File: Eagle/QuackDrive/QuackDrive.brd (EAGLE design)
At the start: 35.9 x 27.9 mm, 102 parts, among them IC1 MCP1703T-3302E/CB, IC10 TB67H450FNG,EL, IC12 TB67H450FNG,EL, IC2 MCP1703T-3302E/CB, IC4 TB67H450FNG,EL, IC6 TB67H450FNG,EL, IC8 TB67H450FNG,EL, Q1 NPN-BJT, Q2 NPN-BJT, U1 MPU-6050-1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

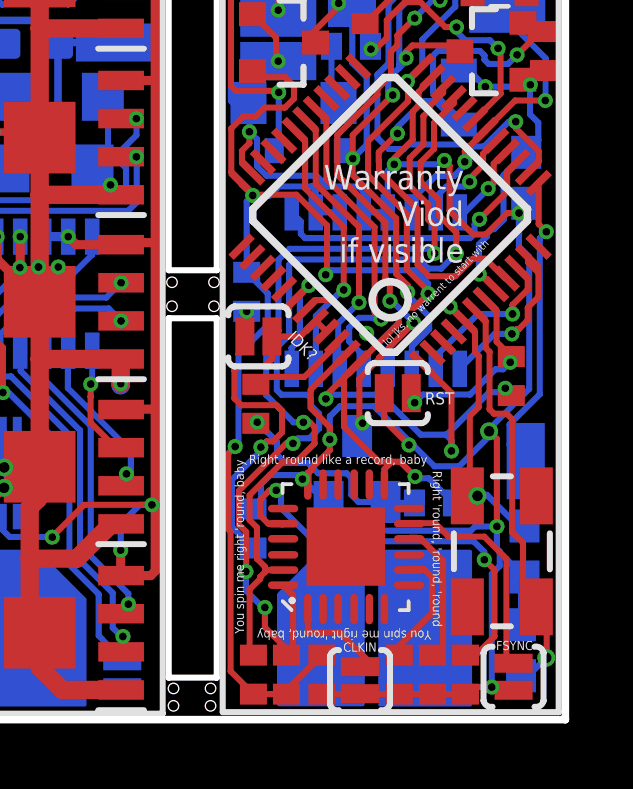
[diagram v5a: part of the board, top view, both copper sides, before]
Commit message: Remove crystal, add Sbus inverter
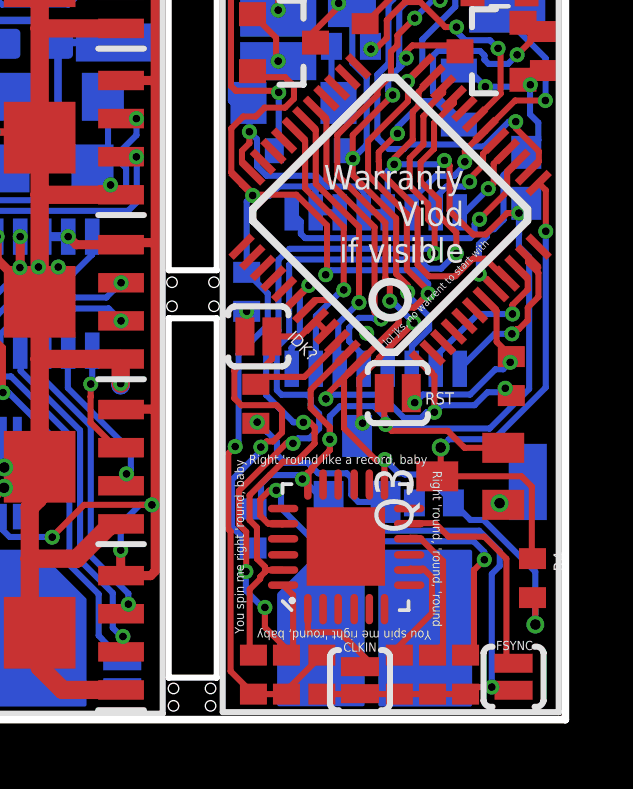
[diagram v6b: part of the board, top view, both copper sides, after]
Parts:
- removed C18, C20: 18pF, SparkFun-Capacitors:0603
- removed OSC: 8MHz, SparkFun2:CRYSTAL-SMD-5X3
- added Q3: (no value), adafruit:SOT23
- added R4: 1k, SparkFun:C0402
- moved PAD23 0.70 mm to (35.6, 9.64)
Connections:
- removed net 8: PAD23.1, UC1.13
- new net N$3: PAD23.1, Q3.1
- new net N$4: Q3.3, R4.1, UC1.13
- net GND: now also Q3.2; no longer C18.1, C20.1
- net OSC_IN: no longer C20.2, OSC.3
- net OSC_OUT: no longer C18.2, OSC.1
- net VCC: now also R4.2
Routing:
- net N$4: track 0.00 -> 18.0 mm, vias 0 -> 2
- net OSC_OUT: track 13.9 -> 0.00 mm, vias 1 -> 0
- net 8: track 10.1 -> 0.00 mm, vias 1 -> 0
- net OSC_IN: track 9.59 -> 0.03 mm, vias 2 -> 0
- net GND: track 104.1 -> 99.6 mm, vias 15 -> 13
- net VCC: track 86.1 -> 89.6 mm, vias 10 -> 11
- net N$3: track 0.00 -> 1.38 mm, vias 0 -> 1

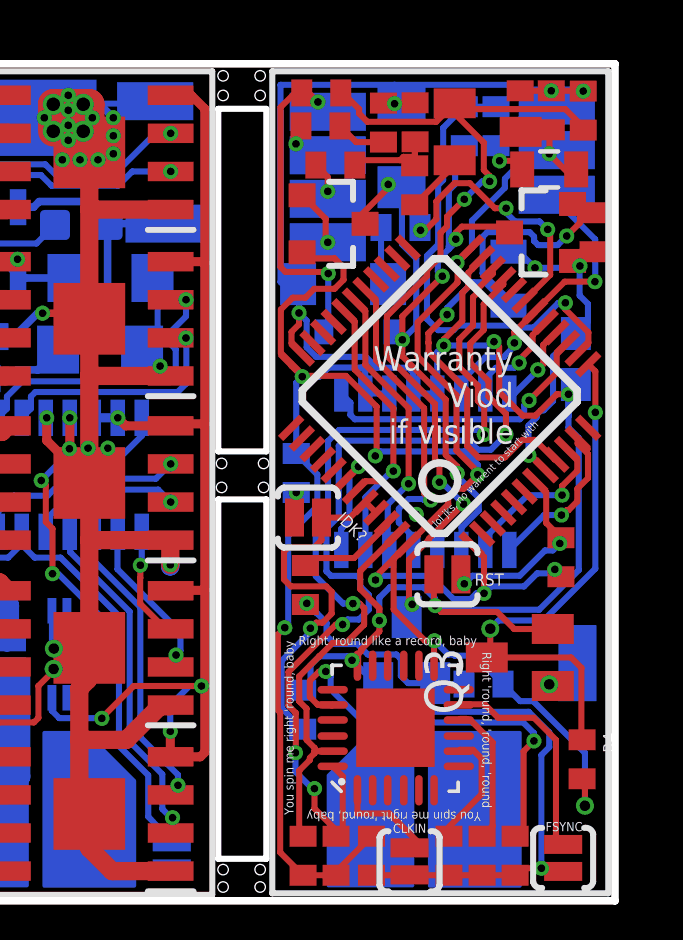
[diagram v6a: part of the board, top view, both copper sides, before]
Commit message: fixed silksceeen
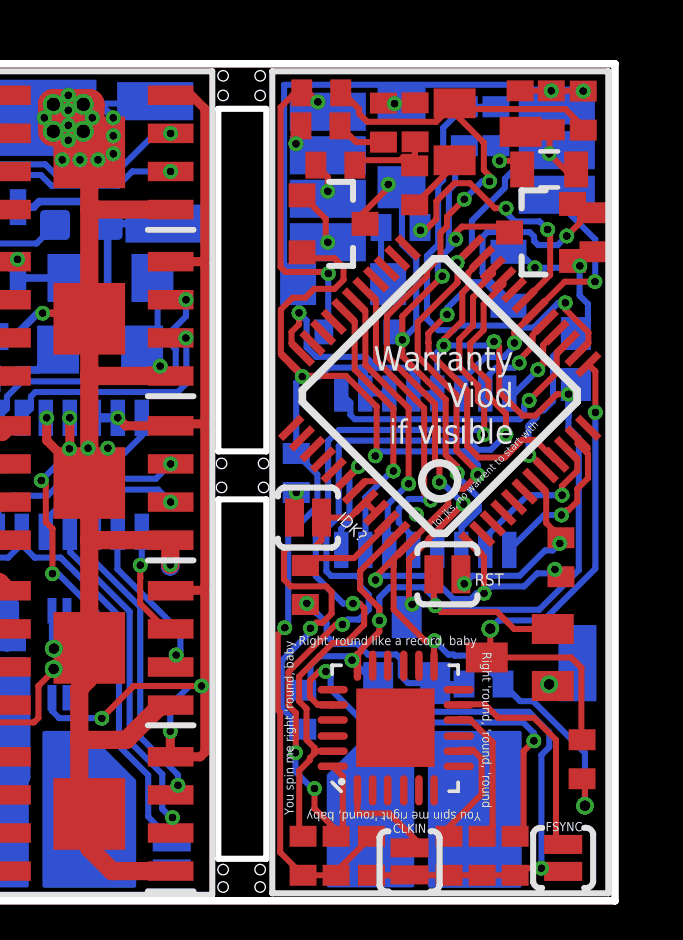
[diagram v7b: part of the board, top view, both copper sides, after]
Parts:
- R4: value 1k -> 4K7
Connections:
- net N$3 renamed SBUSIN
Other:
- board text added: "Never gonna give you up Never gonna let you down Never gonna run around and Never gonna make you cry Never gonna say goodbye Never gonna tell a lie a Never gonna let you Never gonna run ar Never gonna make Never gonna say go Never gonna tell a"
- board text removed: "Never gonna give you up Never gonna let you down Never gonna run around and desert you Never gonna make you cry Never gonna say goodbye Never gonna tell a lie and hurt you Never gonna give you up Never gonna let you down Never gonna run around and desert you Never gonna make you cry Never gonna say goodbye Never gonna tell a lie and hurt you"
- board text removed: "S3G"
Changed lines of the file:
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@@
 <drawing>
 <settings>
-<setting alwaysvectorfont="no"/>
+<setting alwaysvectorfont="yes"/>
 <setting verticaltext="up"/>
 </settings>
@@
 <layer number="15" name="Route15" color="23" fill="1" visible="no" active="no"/>
 <layer number="16" name="Bottom" color="1" fill="1" visible="yes" active="yes"/>
-<layer number="17" name="Pads" color="2" fill="1" visible="yes" active="yes"/>
-<layer number="18" name="Vias" color="2" fill="1" visible="yes" active="yes"/>
-<layer number="19" name="Unrouted" color="6" fill="1" visible="yes" active="yes"/>
-<layer number="20" name="Dimension" color="24" fill="1" visible="yes" active="yes"/>
-<layer number="21" name="tPlace" color="7" fill="1" visible="yes" active="yes"/>
-<layer number="22" name="bPlace" color="7" fill="1" visible="yes" active="yes"/>
-<layer number="23" name="tOrigins" color="15" fill="1" visible="yes" active="yes"/>
-<layer number="24" name="bOrigins" color="15" fill="1" visible="yes" active="yes"/>
+<layer number="17" name="Pads" color="2" fill="1" visible="no" active="yes"/>
+<layer number="18" name="Vias" color="2" fill="1" visible="no" active="yes"/>
+<layer number="19" name="Unrouted" color="6" fill="1" visible="no" active="yes"/>
+<layer number="20" name="Dimension" color="24" fill="1" visible="no" active="yes"/>
+<layer number="21" name="tPlace" color="7" fill="1" visible="no" active="yes"/>
+<layer number="22" name="bPlace" color="7" fill="1" visible="no" active="yes"/>
+<layer number="23" name="tOrigins" color="15" fill="1" visible="no" active="yes"/>
+<layer number="24" name="bOrigins" color="15" fill="1" visible="no" active="yes"/>
 <layer number="25" name="tNames" color="7" fill="1" visible="yes" active="yes"/>
 <layer number="26" name="bNames" color="7" fill="1" visible="yes" active="yes"/>
@@
 <layer number="37" name="tTest" color="7" fill="1" visible="no" active="yes"/>
 <layer number="38" name="bTest" color="7" fill="1" visible="no" active="yes"/>
-<layer number="39" name="tKeepout" color="4" fill="11" visible="yes" active="yes"/>
-<layer number="40" name="bKeepout" color="1" fill="11" visible="yes" active="yes"/>
-<layer number="41" name="tRestrict" color="4" fill="10" visible="yes" active="yes"/>
-<layer number="42" name="bRestrict" color="1" fill="10" visible="yes" active="yes"/>
+<layer number="39" name="tKeepout" color="4" fill="11" visible="no" active="yes"/>
+<layer number="40" name="bKeepout" color="1" fill="11" visible="no" active="yes"/>
+<layer number="41" name="tRestrict" color="4" fill="10" visible="no" active="yes"/>
+<layer number="42" name="bRestrict" color="1" fill="10" visible="no" active="yes"/>
 <layer number="43" name="vRestrict" color="2" fill="10" visible="no" active="yes"/>
 <layer number="44" name="Drills" color="7" fill="1" visible="no" active="yes"/>
@@
 <layer number="49" name="Reference" color="7" fill="1" visible="no" active="yes"/>
 <layer number="50" name="dxf" color="7" fill="1" visible="no" active="no"/>
-<layer number="51" name="tDocu" color="7" fill="1" visible="yes" active="yes"/>
-<layer number="52" name="bDocu" color="7" fill="1" visible="yes" active="yes"/>
+<layer number="51" name="tDocu" color="7" fill="1" visible="no" active="yes"/>
+<layer number="52" name="bDocu" color="7" fill="1" visible="no" active="yes"/>
 <layer number="53" name="tGND_GNDA" color="7" fill="9" visible="no" active="no"/>
 <layer number="54" name="bGND_GNDA" color="1" fill="9" visible="no" active="no"/>
@@
 <hole x="25.1" y="16.3" drill="0.35"/>
 <hole x="25.1" y="15.5" drill="0.35"/>
-<text x="34.85" y="21.74" size="1.016" layer="26" rot="MR90">S3G</text>
 <text x="31.38833125" y="19.842240625" size="1.016" layer="26" rot="MR270" align="bottom-right">G+-5</text>
 <text x="17.922603125" y="25.8454875" size="0.4064" layer="26" rot="MR0">GROUNDDDD</text>
@@
 <text x="3.91773125" y="12.607525" size="0.4064" layer="26" rot="MR45">Never gonna give you up
 Never gonna let you down
-Never gonna run around and desert you
+Never gonna run around and
 Never gonna make you cry
 Never gonna say goodbye
-Never gonna tell a lie and hurt you Never gonna give you up
-Never gonna let you down
-Never gonna run around and desert you
-Never gonna make you cry
-Never gonna say goodbye
-Never gonna tell a lie and hurt you</text>
+Never gonna tell a lie a
+Never gonna let you
+Never gonna run ar
+Never gonna make
+Never gonna say go
+Never gonna tell a</text>
 <rectangle x1="-0.0127" y1="-0.0127" x2="14.3383" y2="0.0127" layer="201"/>
 <rectangle x1="-0.0127" y1="0.0127" x2="14.3383" y2="0.0381" layer="201"/>
@@
 <attribute name="MF" value="Allegro MicroSystems LLC" x="17.794921875" y="9.938446875" size="1.778" layer="28" rot="MR180" display="off"/>
 <attribute name="MP" value="ACS70331EESATR-005B3" x="17.794921875" y="9.938446875" size="1.778" layer="28" rot="MR180" display="off"/>
-<attribute name="NAME" x="15.254921875" y="7.398446875" size="1.27" layer="26" rot="MR180"/>
 <attribute name="PACKAGE" value="WFQFN-12 Allegro MicroSystems LLC" x="17.794921875" y="9.938446875" size="1.778" layer="28" rot="MR180" display="off"/>
 <attribute name="VALUE" x="15.254921875" y="13.748446875" size="1.27" layer="28" rot="MR180"/>
 </element>
-<element name="R4" library="SparkFun" package="C0402" value="1k" x="35.71654375" y="6.437225" smashed="yes" rot="R270">
-<attribute name="NAME" x="36.41504375" y="7.326225" size="0.4064" layer="25" rot="R270"/>
+<element name="R4" library="SparkFun" package="C0402" value="4K7" x="35.71654375" y="6.437225" smashed="yes" rot="R270">
 <attribute name="VALUE" x="34.57354375" y="7.516725" size="0.4064" layer="27" rot="R270"/>
 </element>
 <element name="Q3" library="adafruit" package="SOT23" value="" x="33.6400875" y="9.831" smashed="yes" rot="R90">
-<attribute name="NAME" x="31.7350875" y="7.926" size="1.27" layer="25" rot="R90"/>
 <attribute name="VALUE" x="36.8150875" y="7.926" size="1.27" layer="27" rot="R90"/>
 </element>
@@
 <via x="34.359928125" y="2.805725" extent="1-16" drill="0.254"/>
 <wire x1="33.718971875" y1="2.805725" x2="33.485" y2="2.571753125" width="0.2032" layer="1"/>
-<wire x1="25.66235" y1="22.34765" x2="25.66235" y2="28.92" width="0.2032" layer="16"/>
+<wire x1="25.784815625" y1="22.277584375" x2="25.784815625" y2="28.92" width="0.2032" layer="16"/>
 <contactref element="U$3" pad="13"/>
 <contactref element="U$3" pad="12"/>
-<wire x1="25.66235" y1="28.92" x2="29.459659375" y2="28.92" width="0.2032" layer="16"/>
+<wire x1="25.784815625" y1="28.92" x2="29.459659375" y2="28.92" width="0.2032" layer="16"/>
 <wire x1="29.459659375" y1="28.92" x2="33.49" y2="28.92" width="0.2032" layer="16"/>
 <wire x1="30.89" y1="18.63" x2="30.09" y2="18.63" width="0.2032" layer="16"/>
@@
 <contactref element="PAD17" pad="1"/>
 <wire x1="27.160046875" y1="23.749953125" x2="27.24" y2="23.67" width="0.2032" layer="16"/>
-<wire x1="26.25" y1="22.277584375" x2="25.732415625" y2="22.277584375" width="0.2032" layer="16"/>
-<wire x1="25.732415625" y1="22.277584375" x2="25.66235" y2="22.34765" width="0.2032" layer="16"/>
+<wire x1="26.25" y1="22.277584375" x2="25.784815625" y2="22.277584375" width="0.2032" layer="16"/>
 <wire x1="28.876290625" y1="9.02" x2="28.92" y2="8.976290625" width="0.2032" layer="16"/>
 <wire x1="28.92" y1="8.976290625" x2="29.876290625" y2="8.02" width="0.2032" layer="16"/>
@@
 <wire x1="3.64" y1="6.75" x2="3.64" y2="7.015" width="0.2032" layer="16"/>
 </signal>
-<signal name="N$3">
+<signal name="SBUSIN">
 <contactref element="PAD23" pad="1"/>
 <contactref element="Q3" pad="1"/>

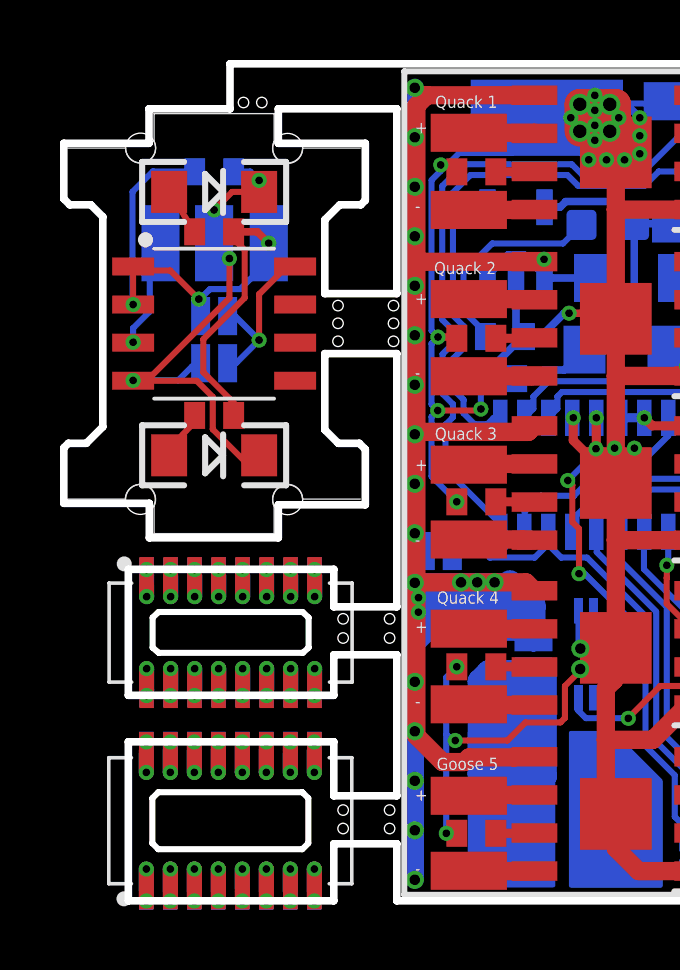
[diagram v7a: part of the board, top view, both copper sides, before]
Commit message: Removed castleation on raiser boards
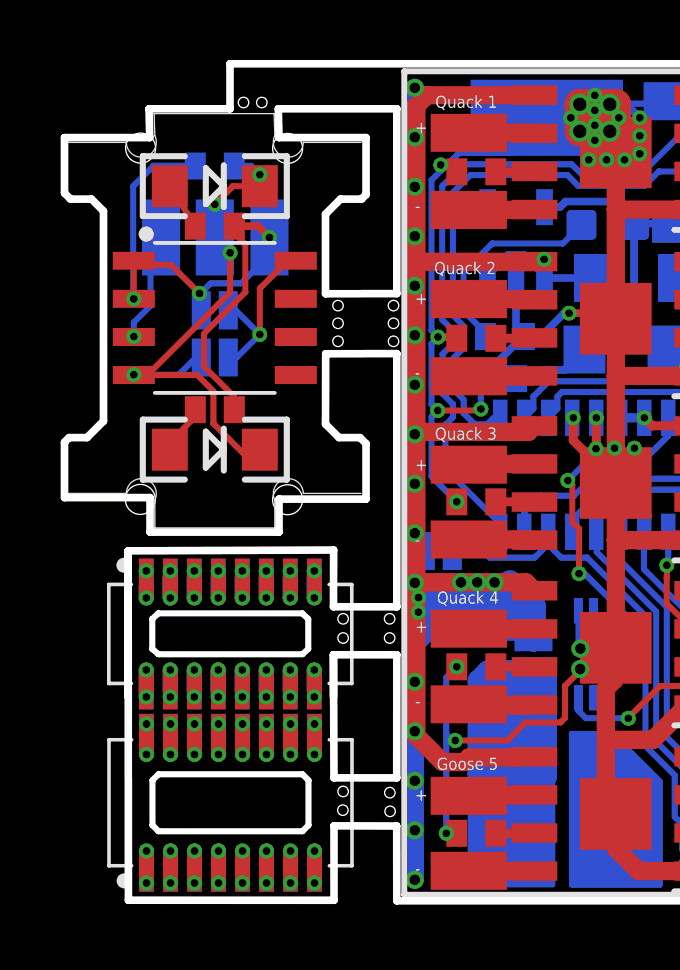
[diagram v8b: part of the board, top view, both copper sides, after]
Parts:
- moved U$8 0.60 mm to (6.45, 4.54)
- moved U$7 0.60 mm to (6.45, 5.44)
- moved C15 0.19 mm to (5.92, 26.2)
- moved D4 0.19 mm to (5.92, 16.8)
- moved R21 0.19 mm to (5.92, 24.2)
- moved R24 0.19 mm to (5.92, 18.1)
- moved D3 0.19 mm to (5.92, 25.5)
- moved PAD13 0.19 mm to (4.13, 23.8)
- moved PAD4 0.19 mm to (5.92, 23.8)
- moved PAD7 0.19 mm to (7.74, 23.8)
- moved SJ7 0.19 mm to (5.92, 19.8)
- moved SJ8 0.19 mm to (5.92, 21.4)
- moved U4 0.19 mm to (5.92, 21.2)
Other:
- outline, holes or cut-outs redrawn
